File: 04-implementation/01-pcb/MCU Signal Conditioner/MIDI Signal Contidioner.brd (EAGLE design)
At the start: 78 x 31.5 mm, 26 parts, among them J2 ARDUINO-CONN-8X2, J3 ARDUINO-CONN-8X2, U4 24CS01, U6 MCP1700-SOT89, X1 SSW-107-02-S-D, X2 SSW-107-02-S-D, X3 SSW-107-02-S-D, X4 SSW-107-02-S-D, X5 MINI-USB-SHIELD-32005-201

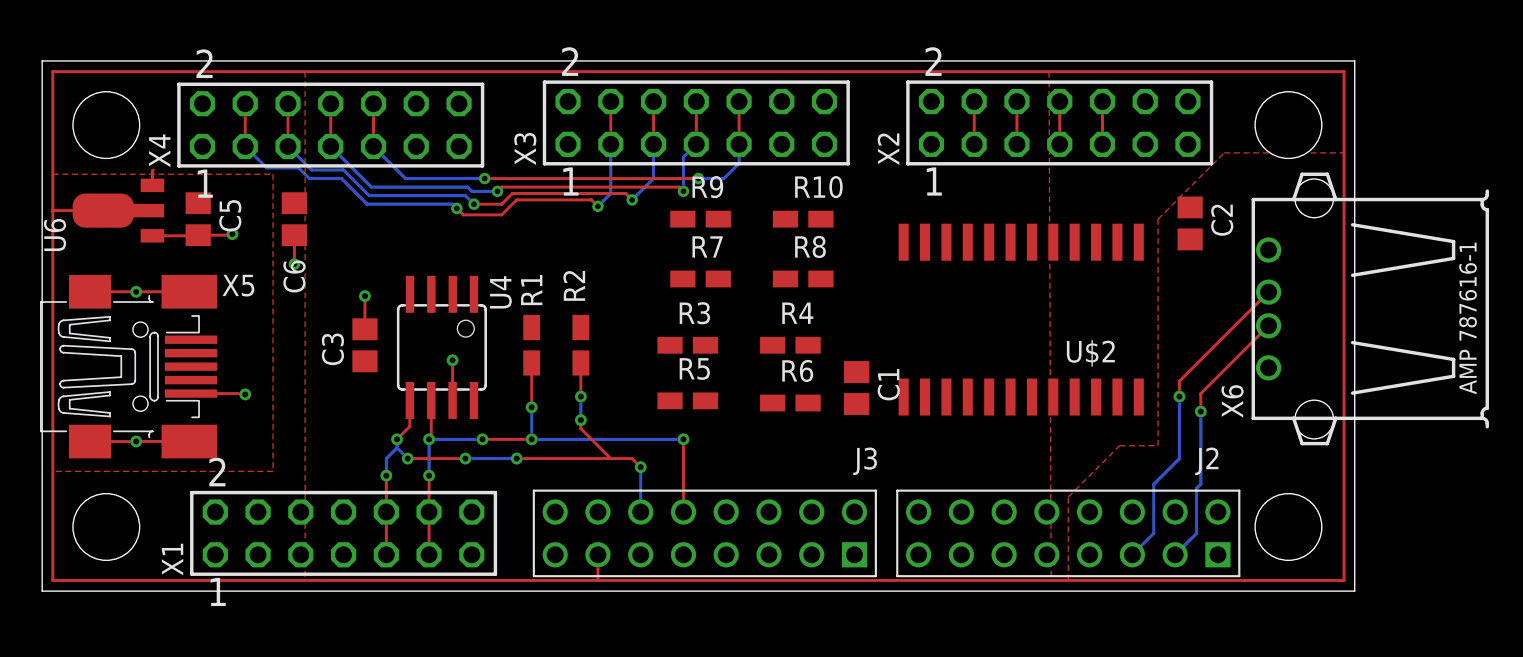
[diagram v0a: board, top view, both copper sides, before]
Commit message: Complete layout of signal conditioner board.
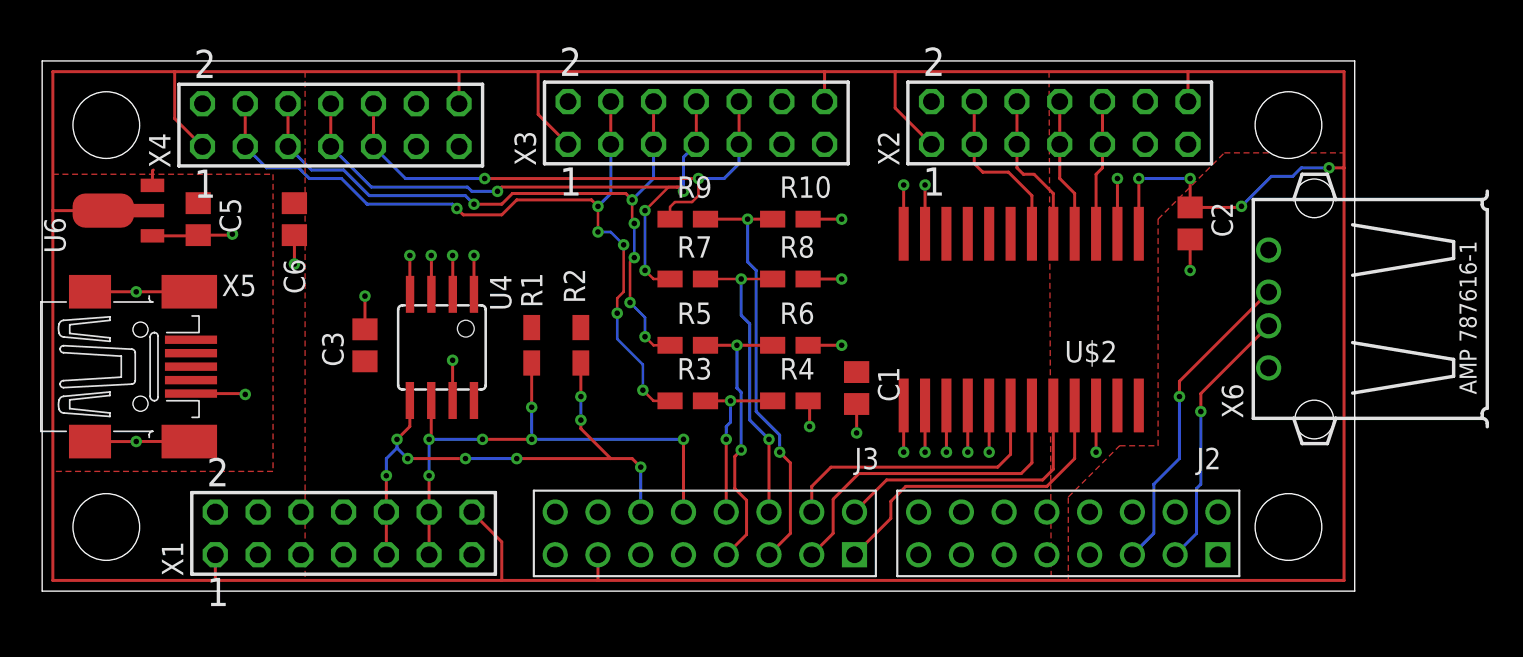
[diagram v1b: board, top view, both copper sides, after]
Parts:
- moved R6 3.43 mm to (44.5, 14.6)
- moved R3 3.30 mm to (38.4, 11.3)
- moved R4 3.30 mm to (44.5, 11.3)
- moved R5 3.30 mm to (38.4, 14.6)
- moved R10 0.76 mm to (44.5, 22.1)
- moved R7 0.76 mm to (38.4, 18.5)
- moved R8 0.76 mm to (44.5, 18.5)
- moved R9 0.76 mm to (38.4, 22.1)
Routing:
- net GND: track 26.0 -> 72.1 mm, vias 7 -> 26
- net +5V: track 218.4 -> 263.7 mm, vias 0 -> 4
- net DI4-3V: track 0.00 -> 25.5 mm, vias 0 -> 2
- net DO2-3V: track 0.00 -> 19.9 mm
- net DO4-3V: track 0.00 -> 19.2 mm
- net DI3-3V: track 0.00 -> 18.5 mm, vias 0 -> 2
- net DI2-3V: track 0.00 -> 17.5 mm, vias 0 -> 2
- net DO1-3V: track 0.00 -> 17.0 mm
- net DO3-3V: track 0.00 -> 16.7 mm
- net DI1: track 32.2 -> 46.9 mm, vias 2 -> 6
- net DI1-3V: track 0.00 -> 10.7 mm, vias 0 -> 2
- net DI2: track 31.2 -> 41.5 mm, vias 2 -> 6
- net DI3: track 30.5 -> 38.2 mm, vias 2 -> 4
- net DO1: track 2.54 -> 10.2 mm
- net DO2: track 2.54 -> 9.12 mm
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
